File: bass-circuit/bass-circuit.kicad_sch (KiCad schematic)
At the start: 26 parts, among them U1 RC4558

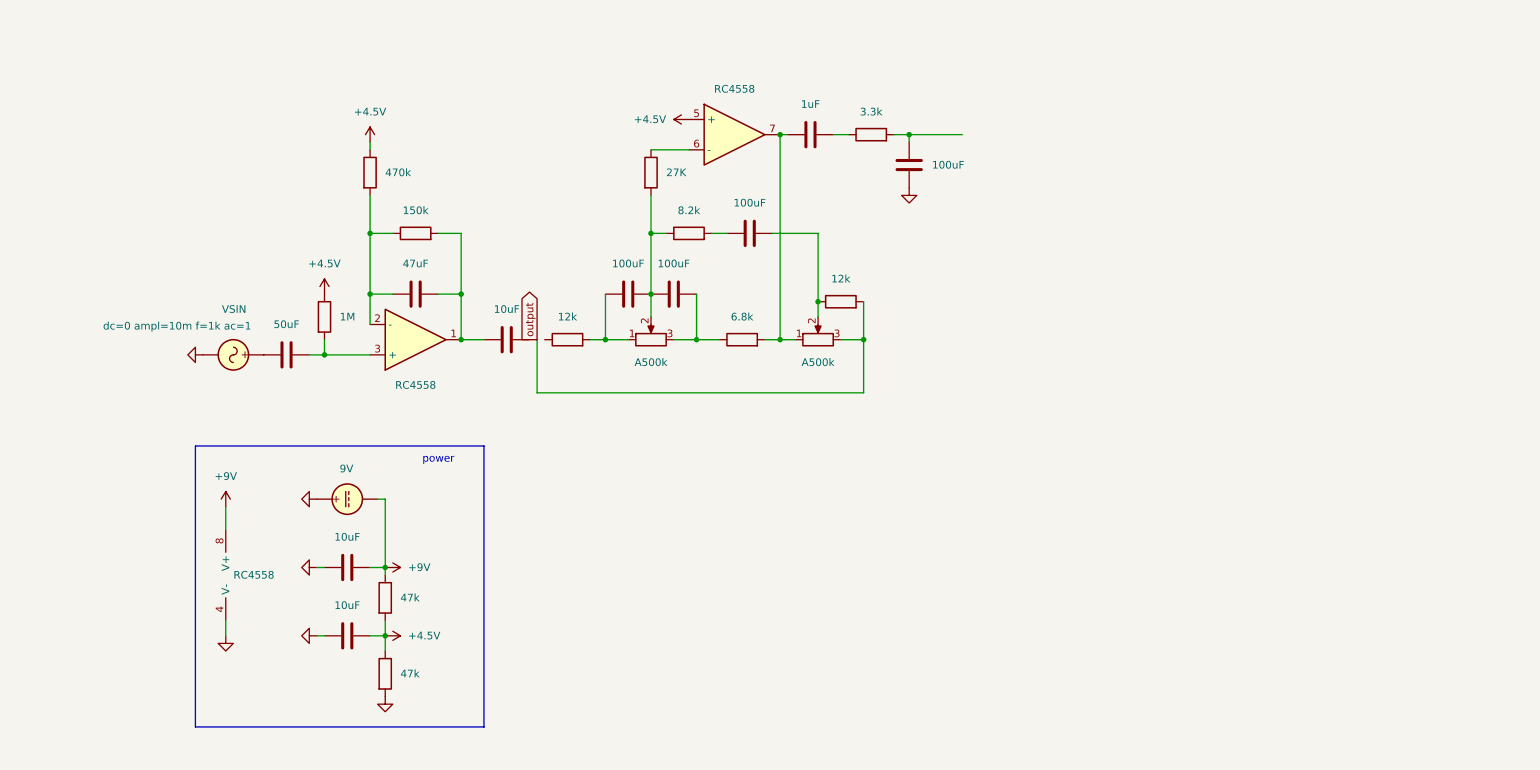
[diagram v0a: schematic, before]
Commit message: pedals and ics added
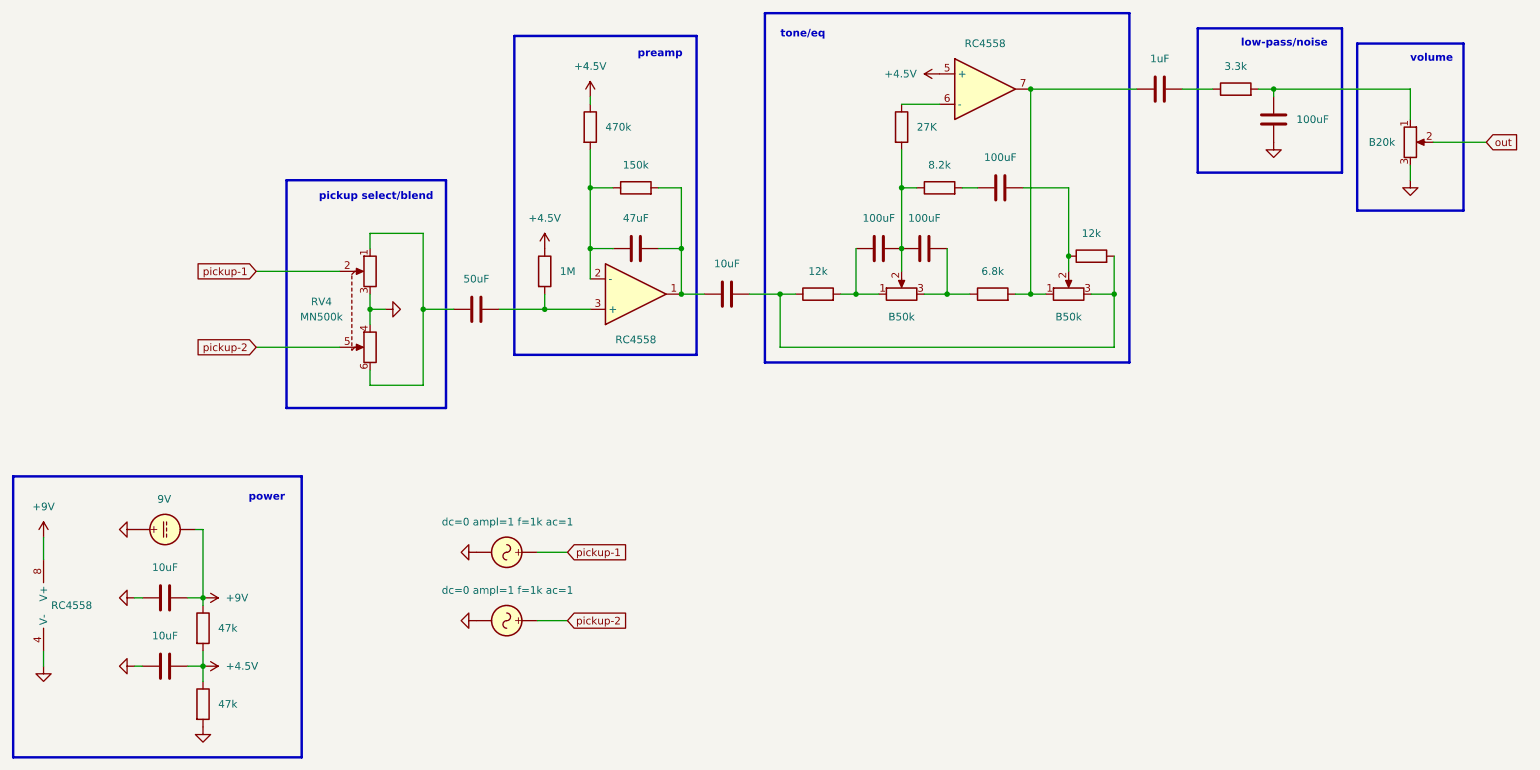
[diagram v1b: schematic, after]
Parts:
- added RV3: B20k, symbol Device:R_Potentiometer
- added RV4: MN500k, symbol Device:R_Potentiometer_Dual
- added V3: VSIN, symbol Simulation_SPICE:VSIN
- RV1, RV2: value A500k -> B50k
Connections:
- net output is gone; now on an unnamed net: C3.2
- net GND: now also RV3.3, RV4.3, RV4.4, V3.2
- net at R2.1: now also R7.2, RV2.3
- net at C1.1: now also RV4.1, RV4.6; no longer V1.1
- net at C9.2, R8.2: now also RV3.1
- new net out: RV3.2
- new net pickup-1: RV4.2, V1.1
- new net pickup-2: RV4.5, V3.1
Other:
- note added: "low-pass/noise"
- note added: "pickup select/blend"
- note added: "preamp"
- note added: "tone/eq"
- note added: "volume"
